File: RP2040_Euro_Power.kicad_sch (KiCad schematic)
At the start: 165 parts, among them J1 Conn_01x40, J2 Conn_01x40, J3 Power, J4 USB C/USB 2.0, J5 Conn_01x03_Pin, SW1 SW_BOOT, SW2 SW_RESET, U1 78L05_SOT89, U101 TL431A, U2 W25Q128JVS, U4 AMS1117-3.3, U5 RP2040, U7 TL072, Y1 Crystal_12MHz_4Pin

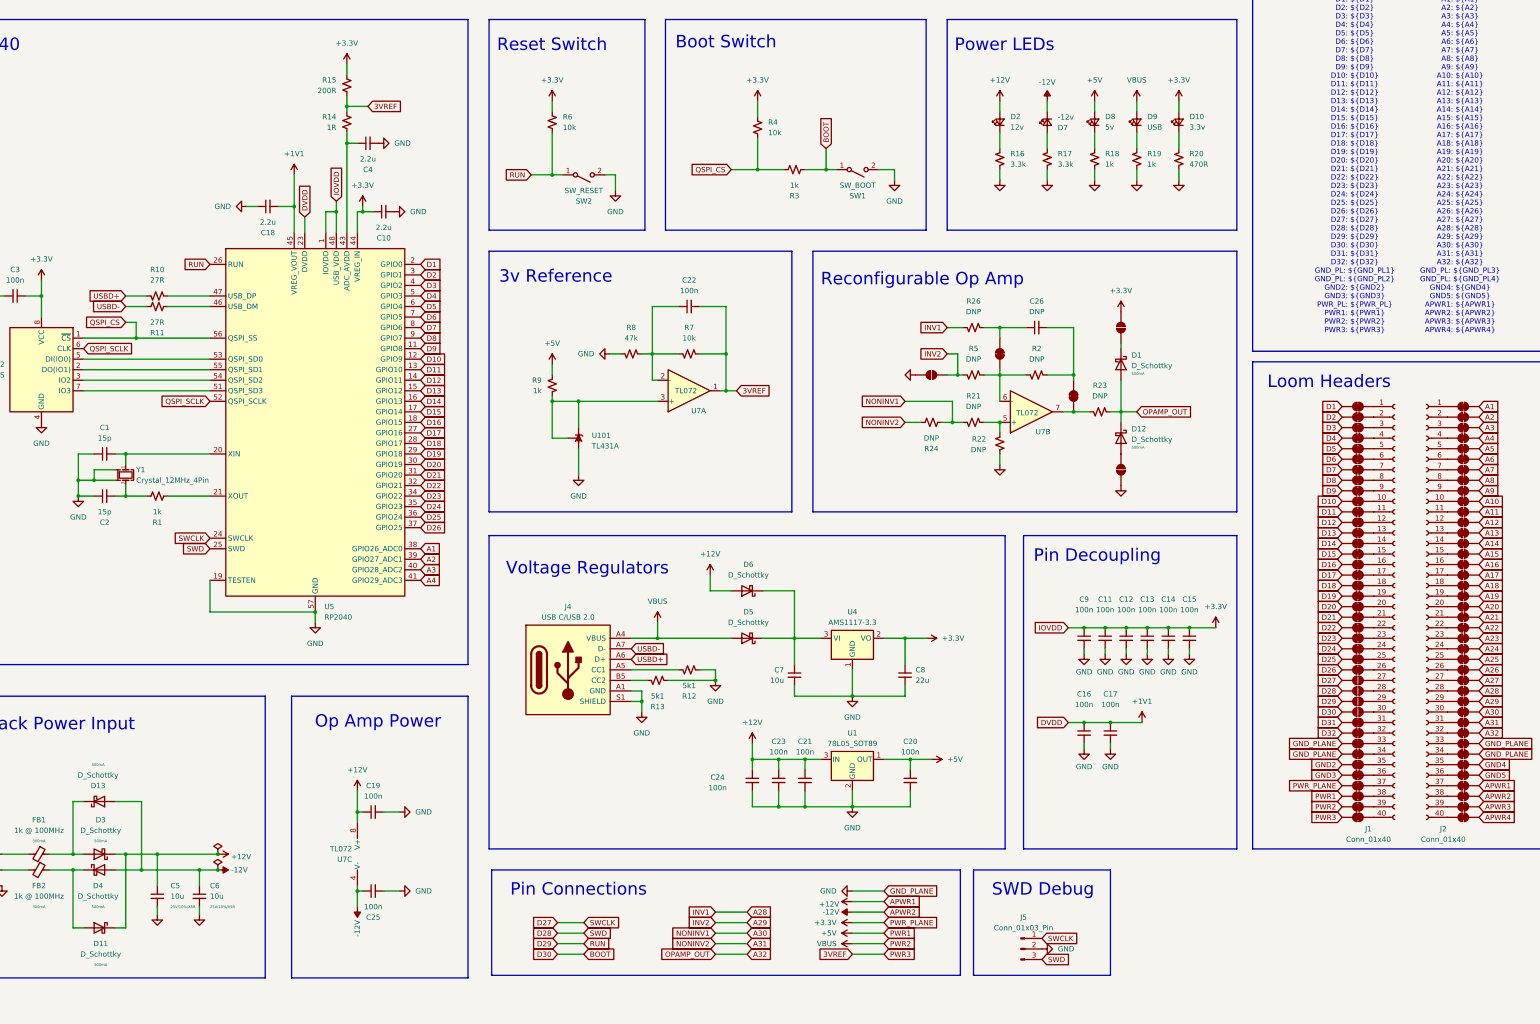
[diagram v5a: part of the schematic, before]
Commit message: Moved buttons to the side, disconnected opamp
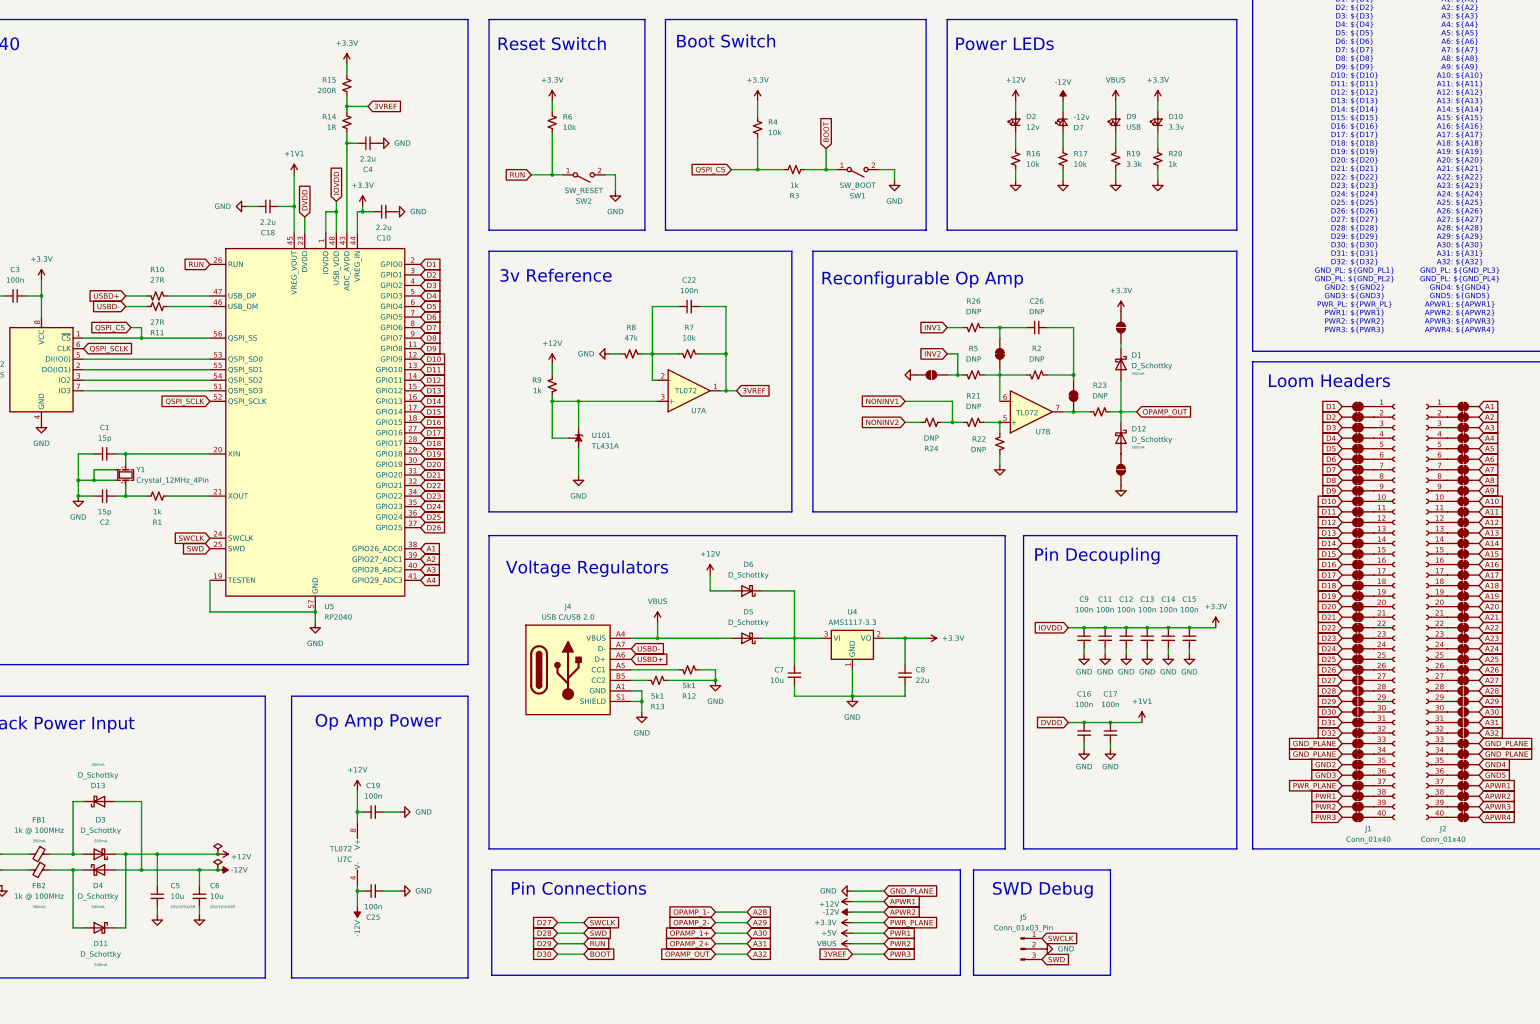
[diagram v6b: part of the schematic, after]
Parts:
- removed C20, C21, C23, C24: 100n, winterbloom:C_0603_HandSolder, symbol DecapodDevices:C_Small
- removed D8: 5v, LED_SMD:LED_0805_2012Metric, symbol Device:LED_Small
- removed JP168, JP169, JP170, JP171, JP172: ~, Decapod_Devices:SolderJumper-2_P1.3mm_Bridged_RoundedPad1.0x1.5mm, symbol Jumper:SolderJumper_2_Bridged
- removed R18: 1k, winterbloom:R_0603_HandSolder, symbol DecapodDevices:R_Small_US
- removed U1: 78L05_SOT89, Package_TO_SOT_SMD:SOT-89-3, symbol Regulator_Linear:L78L05_SOT89
- added JP168, JP169, JP170, JP171, JP172: SolderJumper_2_Open, Decapod_Devices:SolderJumper-2_P1.3mm_Open_Pad1.0x1.5mm, symbol Jumper:SolderJumper_2_Open
- R16, R17: value 3.3k -> 10k; LCSC C22978 -> C25804; MPN 0603WAF3301T5E -> 0603WAF1002T5E
- R19: value 1k -> 3.3k; LCSC C21190 -> C22978; MPN 0603WAF1001T5E -> 0603WAF3301T5E
- R20: value 470R -> 1k; LCSC C23179 -> C21190; MPN 0603WAF4700T5E -> 0603WAF1001T5E
- SW1, SW2: footprint winterbloom:Tactile_Switch_4.2mm -> Decapod_Devices:SW-SMD_TS24CA
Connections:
- net +12V: now also R9.1
- net +5V: no longer R9.1
- net A28: now also JP168.2 (B); no longer R26.1
- net A29: now also JP169.2 (B); no longer JP2.2 (B), R5.1
- net A30: now also JP170.2 (B); no longer R21.1, R24.2
- net A31: now also JP171.2 (B); no longer R24.1
- net A32: now also JP172.2 (B)
- net GND: now also R16.1, R17.1; no longer R16.2, R17.2
- net at J2.28 (Pin_28): now also JP168.1 (A)
- net at D7.2 (A): now also R17.2; no longer R17.1
- net at J2.29 (Pin_29): now also JP169.1 (A)
- net at J2.30 (Pin_30): now also JP170.1 (A)
- net at J2.31 (Pin_31): now also JP171.1 (A)
- net at J2.32 (Pin_32): now also JP172.1 (A)
- net at D2.1 (K): now also R16.2; no longer R16.1
- new net INV1: R26.1
- new net INV2: JP2.2 (B), R5.1
- new net NONINV1: R21.1, R24.2
- new net NONINV2: R24.1
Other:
- moved on the sheet: D10, D2, D7, D9

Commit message: Version 2 Basically ready to order
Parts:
- SW1: value SW_BOOT -> BOOT
- SW2: value SW_RESET -> RESET
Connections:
- net INV1 is gone; now on net A28: R26.1
- net INV2 is gone; now on net A29: JP2.2 (B), R5.1
- net NONINV1 is gone; now on net A30: R21.1, R24.2
- net NONINV2 is gone; now on net A31: R24.1
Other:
- note added: "Voltage Regulator"
- note removed: "No Obvious Problems"
- note removed: "Problems"
- note removed: "Prototyping area if extra space? Add Default/RGB LEDs? Add any pin protection? USB? gpio? Test Points? Are all the required test points already exposed to pins?"
- note removed: "TODO"
- note removed: "Voltage Regulators"
- moved on the sheet: C7, C8, D5, D6, J4, R12, R13, U4

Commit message: Version 2 ready to order
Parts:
- SW1, SW2: LCSC C139797 -> C393942; MPN SKRPACE010 -> TS24CA; Manufacturer ALPSALPINE -> SHOU HAN
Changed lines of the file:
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@@
 			)
 		)
-		(property "LCSC" "C139797"
+		(property "LCSC" "C393942"
 			(at 247.65 68.58 0)
 			(effects
@@
 			)
 		)
-		(property "MPN" "SKRPACE010"
+		(property "MPN" "TS24CA"
 			(at 247.65 68.58 0)
 			(effects
@@
 			)
 		)
-		(property "Manufacturer" "ALPSALPINE "
+		(property "Manufacturer" "SHOU HAN"
 			(at 247.65 68.58 0)
 			(effects
@@
 			)
 		)
-		(property "LCSC" "C139797"
+		(property "LCSC" "C393942"
 			(at 181.61 69.85 0)
 			(effects
@@
 			)
 		)
-		(property "MPN" "SKRPACE010"
+		(property "MPN" "TS24CA"
 			(at 181.61 69.85 0)
 			(effects
@@
 			)
 		)
-		(property "Manufacturer" "ALPSALPINE "
+		(property "Manufacturer" "SHOU HAN"
 			(at 181.61 69.85 0)
 			(effects
